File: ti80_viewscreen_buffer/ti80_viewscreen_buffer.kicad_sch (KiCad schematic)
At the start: 7 parts

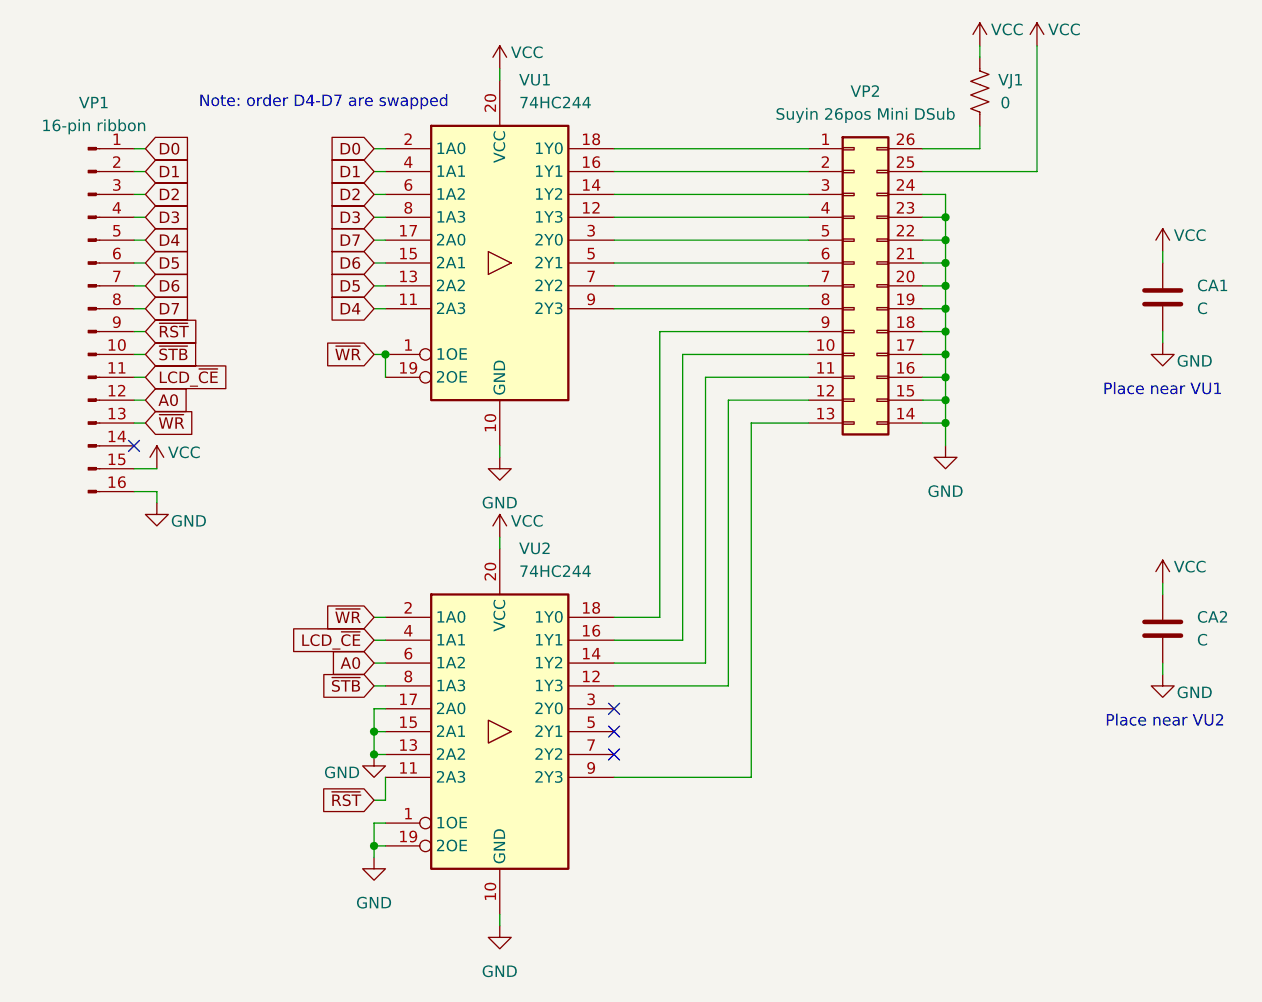
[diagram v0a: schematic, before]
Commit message: Correct pinouts of TI80 viewscreen buffer board
- 74HC244 is Toshiba which numbers 1-4 and 2nd block starts pin 11
- 26-pin half pitch ultra thin D-Sub is top-down order
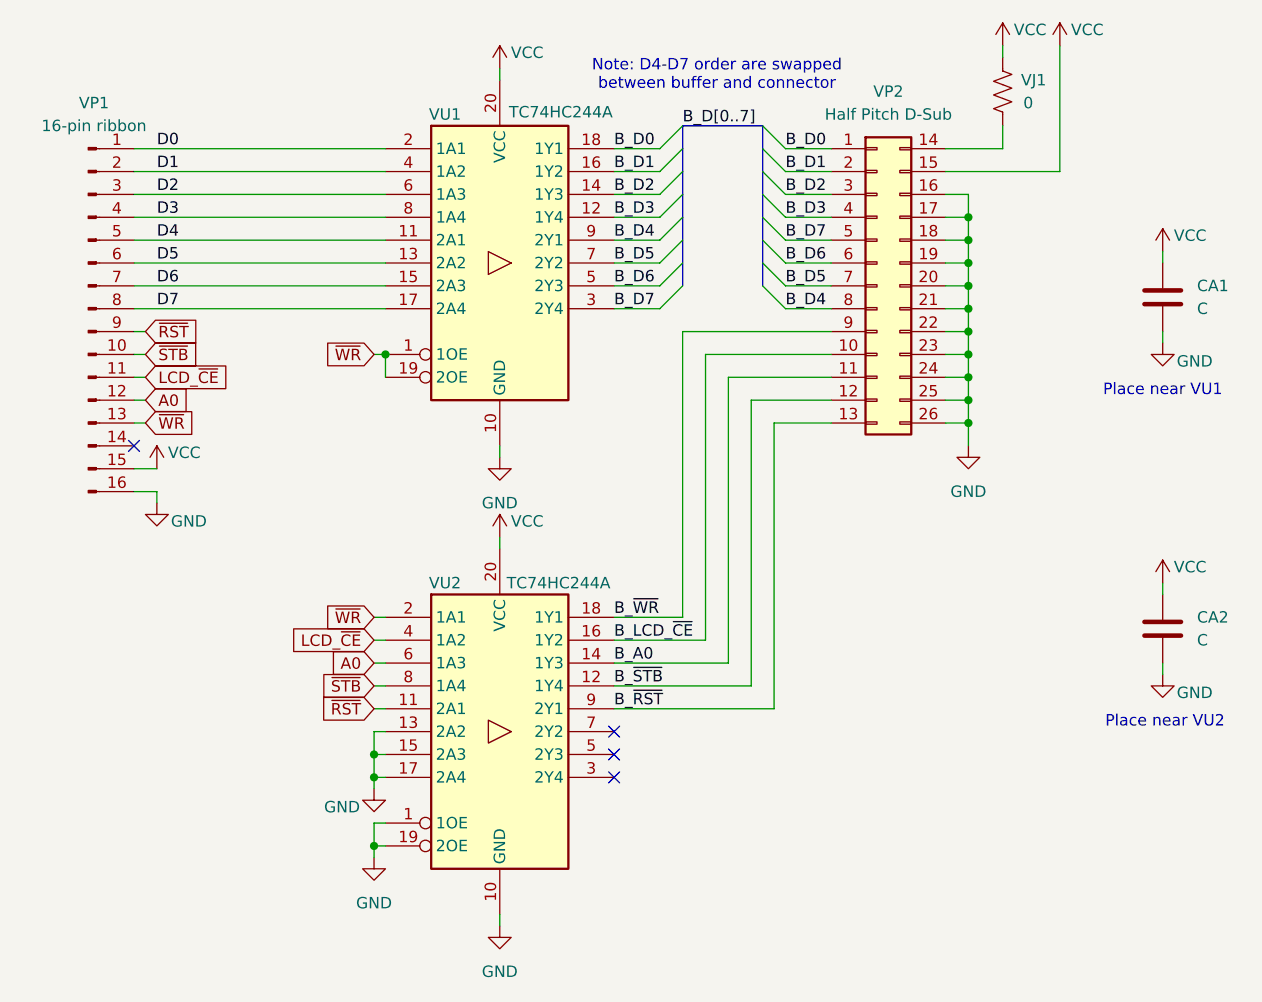
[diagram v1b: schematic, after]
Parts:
- removed VP2: Suyin 26pos Mini DSub, symbol Connector_Generic:Conn_02x13_Counter_Clockwise
- removed VU1, VU2: 74HC244, symbol 74xx:74HC244
- added VP2: Half Pitch D-Sub, symbol Connector_Generic:Conn_02x13_Top_Bottom
- added VU1, VU2: TC74HC244A, Package_SO:SOP-20_7.5x12.8mm_P1.27mm, symbol Toshiba_74xx:TC74HC244A
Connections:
- net A0: now also VU2.6 (1A3)
- net D0: now also VU1.2 (1A1)
- net D1: now also VU1.4 (1A2)
- net D2: now also VU1.6 (1A3)
- net D3: now also VU1.8 (1A4)
- net D4: now also VU1.11 (2A1)
- net D5: now also VU1.13 (2A2)
- net D6: now also VU1.15 (2A3)
- net D7: now also VU1.17 (2A4)
- net GND: now also VP2.16 (Pin_16), VP2.17 (Pin_17), VP2.18 (Pin_18), VP2.19 (Pin_19), VP2.20 (Pin_20), VP2.21 (Pin_21), VP2.22 (Pin_22), VP2.23 (Pin_23), VP2.24 (Pin_24), VP2.25 (Pin_25), VP2.26 (Pin_26), VU1.10 (GND), VU2.1 (1OE), VU2.10 (GND), VU2.13 (2A2), VU2.15 (2A3), VU2.17 (2A4), VU2.19 (2OE)
- net LCD_~{CE}: now also VU2.4 (1A2)
- net VCC: now also VP2.15 (Pin_15), VU1.20 (VCC), VU2.20 (VCC)
- net ~{RST}: now also VU2.11 (2A1)
- net ~{STB}: now also VU2.8 (1A4)
- net ~{WR}: now also VU1.1 (1OE), VU1.19 (2OE), VU2.2 (1A1)
- net at VJ1.2: now also VP2.14 (Pin_14)
- new net B_A0: VP2.11 (Pin_11), VU2.14 (1Y3)
- new net B_D0: VP2.1 (Pin_1), VU1.18 (1Y1)
- new net B_D1: VP2.2 (Pin_2), VU1.16 (1Y2)
- new net B_D2: VP2.3 (Pin_3), VU1.14 (1Y3)
- new net B_D3: VP2.4 (Pin_4), VU1.12 (1Y4)
- new net B_D4: VP2.8 (Pin_8), VU1.9 (2Y1)
- new net B_D5: VP2.7 (Pin_7), VU1.7 (2Y2)
- new net B_D6: VP2.6 (Pin_6), VU1.5 (2Y3)
- new net B_D7: VP2.5 (Pin_5), VU1.3 (2Y4)
- new net B_LCD_~{CE}: VP2.10 (Pin_10), VU2.16 (1Y2)
- new net B_~{RST}: VP2.13 (Pin_13), VU2.9 (2Y1)
- new net B_~{STB}: VP2.12 (Pin_12), VU2.12 (1Y4)
- new net B_~{WR}: VP2.9 (Pin_9), VU2.18 (1Y1)
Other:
- note added: "Note: D4-D7 order are swapped between buffer and connector"
- note removed: "Note: order D4-D7 are swapped"
- moved on the sheet: VJ1
